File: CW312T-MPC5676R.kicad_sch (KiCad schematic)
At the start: 0 parts

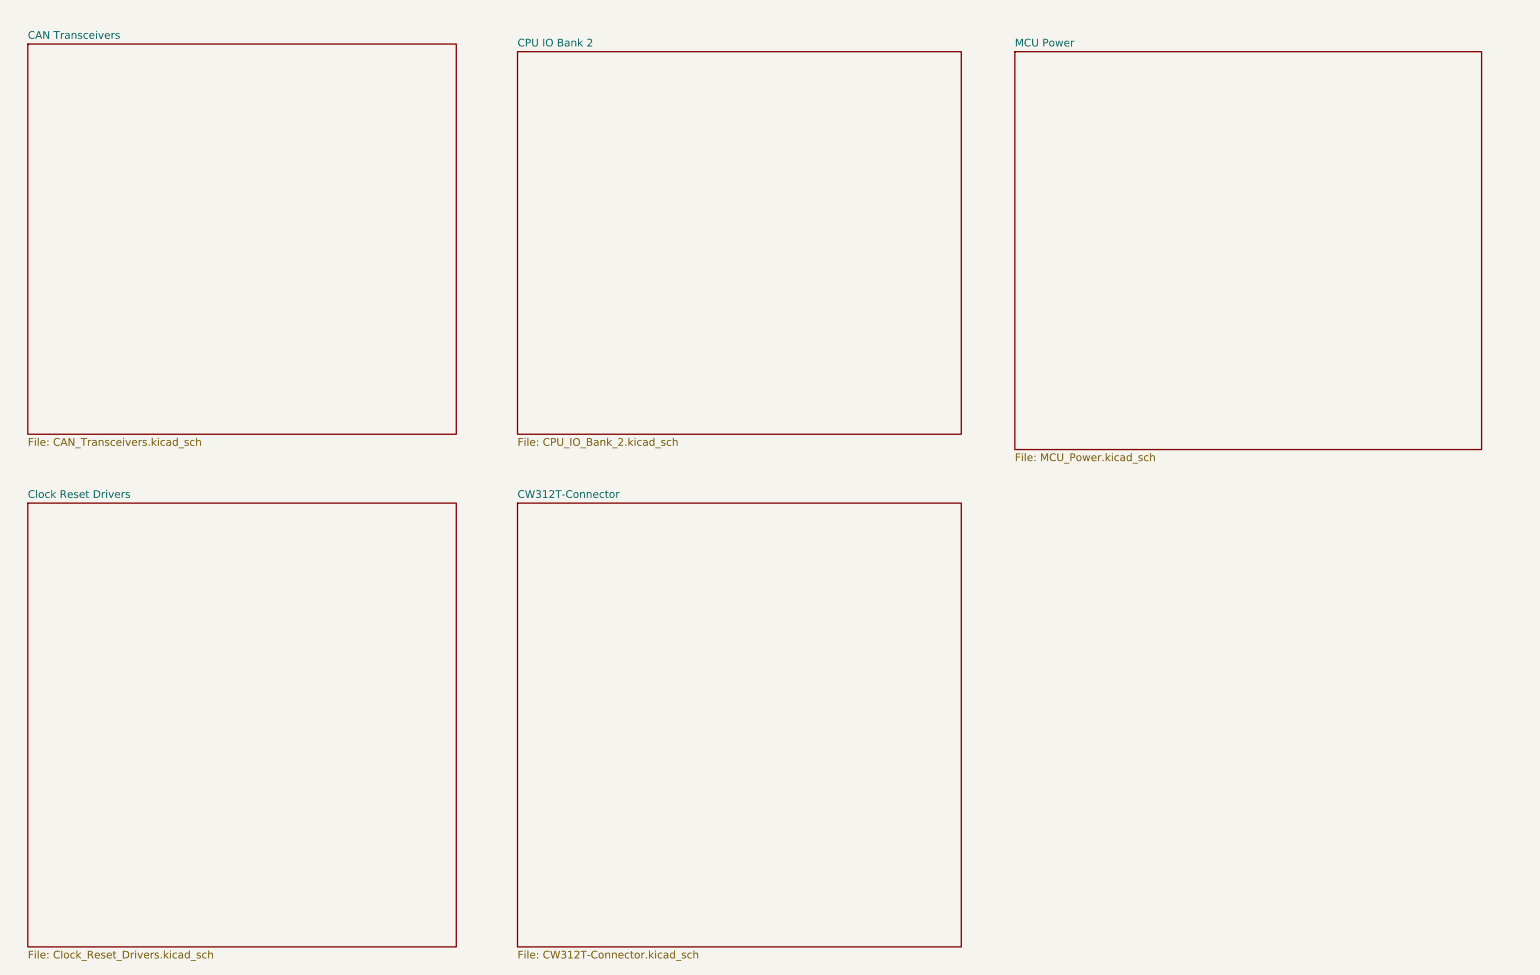
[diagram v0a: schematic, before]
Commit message: draft updated, schematic draft done, pcb issues with size of board and fitting all parts on
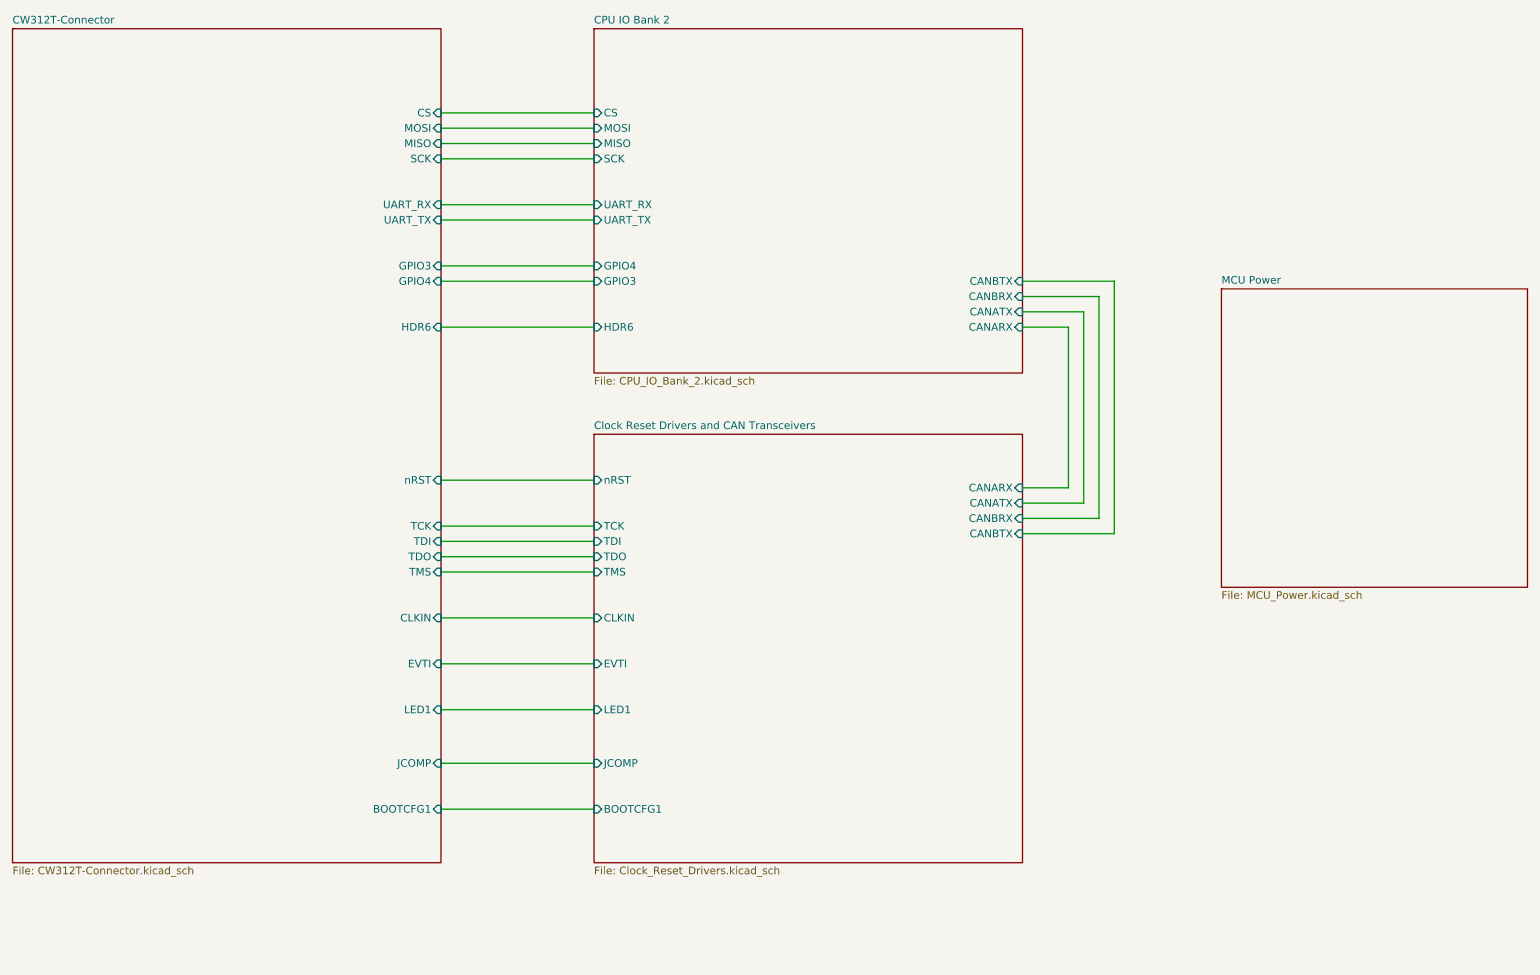
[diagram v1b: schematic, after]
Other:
- sheet Clock Reset Drivers renamed Clock Reset Drivers and CAN Transceivers
- removed sheet CAN Transceivers
- sheet CPU IO Bank 2 ports: added CANARX, CANATX, CANBRX, CANBTX, CS, GPIO3, GPIO4, HDR6, MISO, MOSI, SCK, UART_RX, UART_TX; removed none
- sheet CW312T-Connector ports: added BOOTCFG1, CLKIN, CS, EVTI, GPIO3, GPIO4, HDR6, JCOMP, LED1, MISO, MOSI, SCK, TCK, TDI, TDO, TMS, UART_RX, UART_TX, nRST; removed none
- sheet Clock Reset Drivers and CAN Transceivers ports: added BOOTCFG1, CANARX, CANATX, CANBRX, CANBTX, CLKIN, EVTI, JCOMP, LED1, TCK, TDI, TDO, TMS, nRST; removed none
